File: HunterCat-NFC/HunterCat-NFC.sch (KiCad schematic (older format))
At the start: 64 parts, among them J1 Battery, P1 USB_C_Plug_USB2.0, SW1 RESET, U1 ATSAMD21E18A, U2 PN7150B0HN_C11002E-PN7150B0HN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, U3 MCP73831-3-OT, U4 AP2112K-3.3, U5 W25Q32JVSS, Y1 27.12Mhz

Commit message: update sheet
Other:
- note removed: "NOTA: Calcular capacitores y resistencias!!\nSegun datasheet"
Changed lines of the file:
@@
 Comment1 ""
 Comment2 ""
-Comment3 ""
+Comment3 "Eduardo Contreras"
 Comment4 "Andres Sabas"
 $EndDescr
@@
 Wire Notes Line
 	5720 3405 11210 3405
-Text Notes 9495 1500 0    50   ~ 0
-NOTA: Calcular capacitores y resistencias!!\nSegun datasheet
 $Comp
 L HunterCat-NFC-rescue:ATSAMD21E18A-Electronic_Cats U1

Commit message: fix GND crystal
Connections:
- net GND: now also Y1.2, Y1.4
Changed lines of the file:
@@
 Wire Wire Line
 	1410 2540 1860 2540
+$Comp
+L power:GND #PWR?
+U 1 1 5EA8FB0C
+P 980 2780
+F 0 "#PWR?" H 980 2530 50  0001 C CNN
+F 1 "GND" H 985 2607 50  0000 C CNN
+F 2 "" H 980 2780 50  0001 C CNN
+F 3 "" H 980 2780 50  0001 C CNN
+	1    980  2780
+	1    0    0    -1
+$EndComp
+Wire Wire Line
+	980  2780 885  2780
+Wire Wire Line
+	885  2780 885  2495
+Wire Wire Line
+	1085 2495 1085 2780
+Wire Wire Line
+	1085 2780 980  2780
+Connection ~ 980  2780
 $EndSCHEMATC

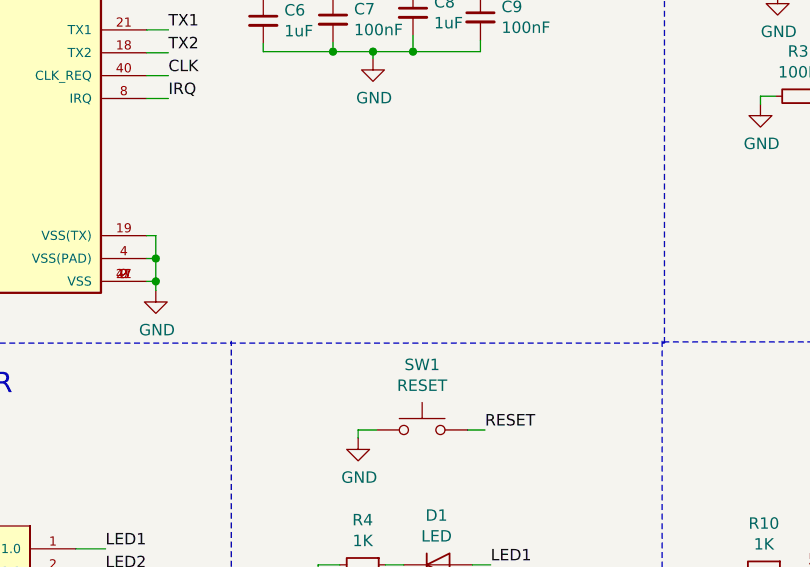
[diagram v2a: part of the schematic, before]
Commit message: add connector test breakout
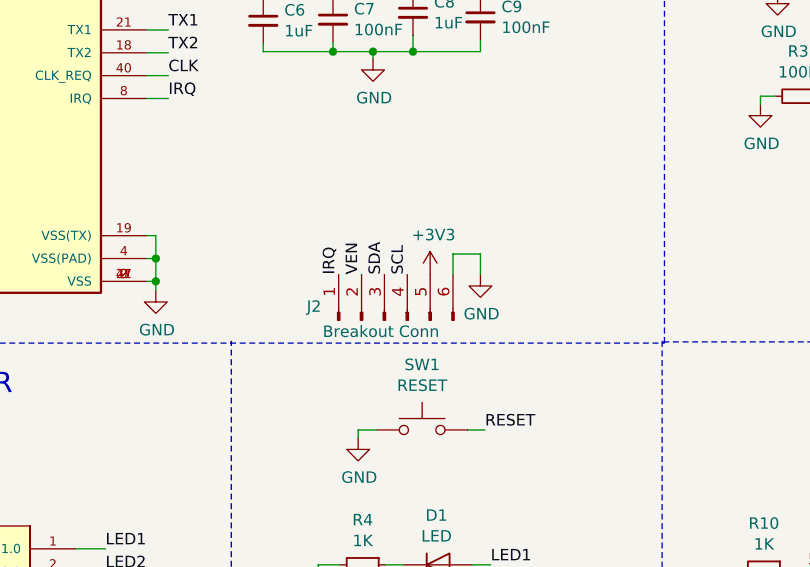
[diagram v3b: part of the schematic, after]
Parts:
- added J2: Breakout Conn, symbol Connector:Conn_01x06_Male
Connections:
- net +3V3: now also J2.5 (Pin_5)
- net GND: now also J2.6 (Pin_6)
- net IRQ: now also J2.1 (Pin_1)
- net SCL: now also J2.4 (Pin_4)
- net SDA: now also J2.3 (Pin_3)
- net VEN: now also J2.2 (Pin_2)
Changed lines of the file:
@@
 	1410 2540 1860 2540
 $Comp
-L power:GND #PWR?
+L power:GND #PWR0105
 U 1 1 5EA8FB0C
 P 980 2780
-F 0 "#PWR?" H 980 2530 50  0001 C CNN
+F 0 "#PWR0105" H 980 2530 50  0001 C CNN
 F 1 "GND" H 985 2607 50  0000 C CNN
 F 2 "" H 980 2780 50  0001 C CNN
@@
 	1085 2780 980  2780
 Connection ~ 980  2780
+$Comp
+L Connector:Conn_01x06_Male J2
+U 1 1 5E87F2EF
+P 4500 3310
+F 0 "J2" V 4560 3650 50  0000 R CNN
+F 1 "Breakout Conn" V 4450 3580 50  0000 R CNN
+F 2 "" H 4500 3310 50  0001 C CNN
+F 3 "~" H 4500 3310 50  0001 C CNN
+	1    4500 3310
+	0    -1   -1   0
+$EndComp
+Text Label 4300 3110 1    50   ~ 0
+IRQ
+Text Label 4400 3110 1    50   ~ 0
+VEN
+Text Label 4500 3110 1    50   ~ 0
+SDA
+Text Label 4600 3110 1    50   ~ 0
+SCL
+$Comp
+L power:+3V3 #PWR0106
+U 1 1 5E8860BE
+P 4700 3110
+F 0 "#PWR0106" H 4700 2960 50  0001 C CNN
+F 1 "+3V3" H 4715 3283 50  0000 C CNN
+F 2 "" H 4700 3110 50  0001 C CNN
+F 3 "" H 4700 3110 50  0001 C CNN
+	1    4700 3110
+	1    0    0    -1
+$EndComp
+$Comp
+L power:GND #PWR0109
+U 1 1 5E887010
+P 4920 3110
+F 0 "#PWR0109" H 4920 2860 50  0001 C CNN
+F 1 "GND" H 4925 2937 50  0000 C CNN
+F 2 "" H 4920 3110 50  0001 C CNN
+F 3 "" H 4920 3110 50  0001 C CNN
+	1    4920 3110
+	1    0    0    -1
+$EndComp
+Wire Wire Line
+	4800 3110 4800 3020
+Wire Wire Line
+	4800 3020 4920 3020
+Wire Wire Line
+	4920 3020 4920 3110
 $EndSCHEMATC

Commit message: update pcb
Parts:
- F1: footprint (none) -> Fuse:Fuse_0805_2012Metric_Pad1.15x1.40mm_HandSolder
- J2: footprint (none) -> Connector_PinSocket_2.54mm:PinSocket_1x06_P2.54mm_Vertical
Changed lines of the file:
@@
 EESchema Schematic File Version 4
+LIBS:HunterCat-NFC-cache
 EELAYER 30 0
 EELAYER END
@@
 F 0 "F1" H 5270 6180 50  0000 C CNN
 F 1 "0.5A" H 5270 6089 50  0000 C CNN
-F 2 "" H 5270 5995 50  0001 C CNN
+F 2 "Fuse:Fuse_0805_2012Metric_Pad1.15x1.40mm_HandSolder" H 5270 5995 50  0001 C CNN
 F 3 "~" H 5270 5995 50  0001 C CNN
 	1    5270 5995
@@
 F 0 "J2" V 4560 3650 50  0000 R CNN
 F 1 "Breakout Conn" V 4450 3580 50  0000 R CNN
-F 2 "" H 4500 3310 50  0001 C CNN
+F 2 "Connector_PinSocket_2.54mm:PinSocket_1x06_P2.54mm_Vertical" H 4500 3310 50  0001 C CNN
 F 3 "~" H 4500 3310 50  0001 C CNN
 	1    4500 3310

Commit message: add footprint crystal and battery connector
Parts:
- J1: footprint (none) -> Connector_PinSocket_2.54mm:PinSocket_2x01_P2.54mm_Vertical
- Y1: footprint (none) -> Crystal:Crystal_SMD_3225-4Pin_3.2x2.5mm_HandSoldering
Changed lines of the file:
@@
 EESchema Schematic File Version 4
-LIBS:HunterCat-NFC-cache
 EELAYER 30 0
 EELAYER END
@@
 F 0 "Y1" V 939 2639 50  0000 L CNN
 F 1 "27.12Mhz" V 860 2115 50  0000 L CNN
-F 2 "" H 985 2495 50  0001 C CNN
+F 2 "Crystal:Crystal_SMD_3225-4Pin_3.2x2.5mm_HandSoldering" H 985 2495 50  0001 C CNN
 F 3 "~" H 985 2495 50  0001 C CNN
 	1    985  2495
@@
 F 0 "J1" H 8505 4152 50  0000 L CNN
 F 1 "Battery" H 8505 4061 50  0000 L CNN
-F 2 "" H 8425 4160 50  0001 C CNN
+F 2 "Connector_PinSocket_2.54mm:PinSocket_2x01_P2.54mm_Vertical" H 8425 4160 50  0001 C CNN
 F 3 "~" H 8425 4160 50  0001 C CNN
 	1    8425 4160

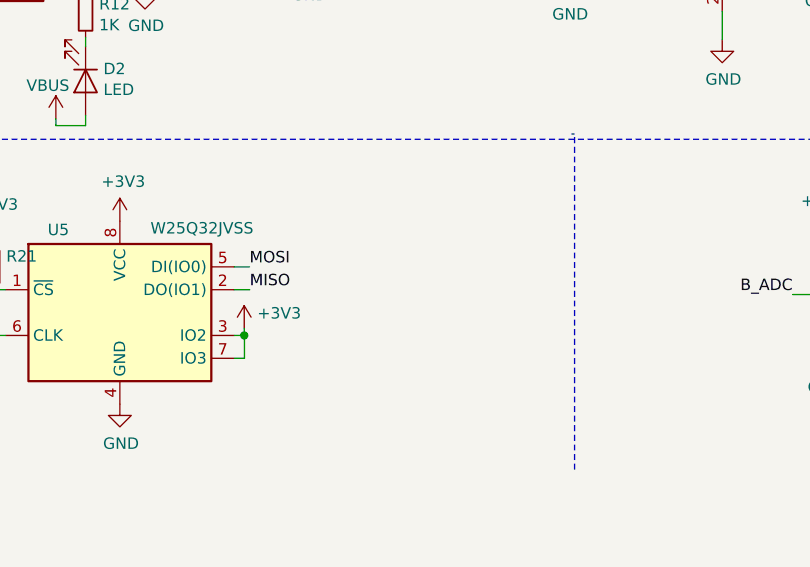
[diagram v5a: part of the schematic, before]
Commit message: add c25
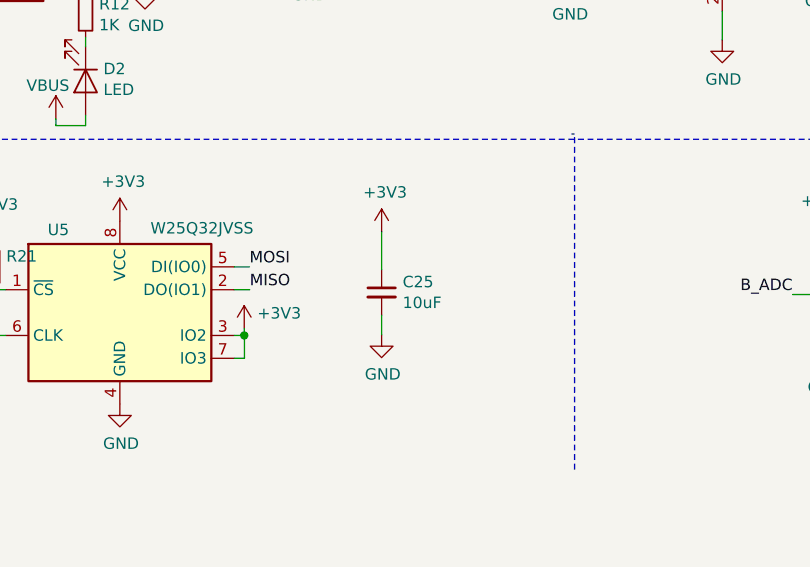
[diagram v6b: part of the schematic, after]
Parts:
- added C25: 10uF, Capacitor_SMD:C_0805_2012Metric_Pad1.15x1.40mm_HandSolder, symbol Device:C_Small
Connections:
- net +3V3: now also C25.1
- net GND: now also C25.2
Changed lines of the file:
@@
 EESchema Schematic File Version 4
+LIBS:HunterCat-NFC-cache
 EELAYER 30 0
 EELAYER END
@@
 Wire Wire Line
 	4920 3020 4920 3110
+$Comp
+L Device:C_Small C25
+U 1 1 5E935CDE
+P 8505 5770
+F 0 "C25" H 8597 5816 50  0000 L CNN
+F 1 "10uF" H 8597 5725 50  0000 L CNN
+F 2 "Capacitor_SMD:C_0805_2012Metric_Pad1.15x1.40mm_HandSolder" H 8505 5770 50  0001 C CNN
+F 3 "~" H 8505 5770 50  0001 C CNN
+	1    8505 5770
+	1    0    0    -1
+$EndComp
+$Comp
+L power:GND #PWR0110
+U 1 1 5E9363B8
+P 8505 5955
+F 0 "#PWR0110" H 8505 5705 50  0001 C CNN
+F 1 "GND" H 8510 5782 50  0000 C CNN
+F 2 "" H 8505 5955 50  0001 C CNN
+F 3 "" H 8505 5955 50  0001 C CNN
+	1    8505 5955
+	1    0    0    -1
+$EndComp
+$Comp
+L power:+3V3 #PWR0111
+U 1 1 5E936E6F
+P 8505 5505
+F 0 "#PWR0111" H 8505 5355 50  0001 C CNN
+F 1 "+3V3" H 8520 5678 50  0000 C CNN
+F 2 "" H 8505 5505 50  0001 C CNN
+F 3 "" H 8505 5505 50  0001 C CNN
+	1    8505 5505
+	1    0    0    -1
+$EndComp
+Wire Wire Line
+	8505 5505 8505 5670
+Wire Wire Line
+	8505 5870 8505 5955
 $EndSCHEMATC

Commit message: value c25
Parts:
- C25: value 10uF -> 0.1uF
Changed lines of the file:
@@
 P 8505 5770
 F 0 "C25" H 8597 5816 50  0000 L CNN
-F 1 "10uF" H 8597 5725 50  0000 L CNN
+F 1 "0.1uF" H 8597 5725 50  0000 L CNN
 F 2 "Capacitor_SMD:C_0805_2012Metric_Pad1.15x1.40mm_HandSolder" H 8505 5770 50  0001 C CNN
 F 3 "~" H 8505 5770 50  0001 C CNN

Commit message: Update SPI Flash and Gerbers settings
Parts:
- U5: value W25Q32JVSS -> GD25Q16CSIGR
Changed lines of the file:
@@
 EESchema Schematic File Version 4
-LIBS:HunterCat-NFC-cache
 EELAYER 30 0
 EELAYER END
@@
 P 7360 5858
 F 0 "U5" H 7091 6220 50  0000 C CNN
-F 1 "W25Q32JVSS" H 7719 6227 50  0000 C CNN
+F 1 "GD25Q16CSIGR" H 7719 6227 50  0000 C CNN
 F 2 "Package_SO:SOIC-8_5.23x5.23mm_P1.27mm" H 7360 5858 50  0001 C CNN
 F 3 "http://www.winbond.com/resource-files/w25q32jv%20revg%2003272018%20plus.pdf" H 7360 5858 50  0001 C CNN
